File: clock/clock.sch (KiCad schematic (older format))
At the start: 4 parts, among them P101 CONN_01X03, P102 CONN_FAN_PWM, P103 CONN_02X08

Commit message: Place the reference designators.
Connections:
- net labels added: ~CARRIER_SRST~
- wire segments 129 -> 133
- no-connect marks 1 -> 0
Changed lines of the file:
@@
 F26 "TEMP_SDA" I R 3500 4500 60
 F27 "FAN_TACH" I L 2400 5500 60
+F28 "~CARRIER_SRST~" I L 2400 5000 60
 $EndSheet
 $Comp
@@
 	1    0    0    -1
 $EndComp
-NoConn ~ 1050 6900
 $Comp
 L PWR_FLAG #FLG07
@@
 Connection ~ 1700 2750
 Wire Wire Line
-	9950 1100 10050 1100
-Wire Wire Line
-	10050 1100 10050 1950
-Wire Wire Line
-	9950 1800 10050 1800
+	10050 1800 9950 1800
 Connection ~ 10050 1800
 Wire Wire Line
-	9950 1700 10050 1700
+	10050 1700 9950 1700
 Connection ~ 10050 1700
 Wire Wire Line
-	9950 1600 10050 1600
+	10050 1600 9950 1600
 Connection ~ 10050 1600
 Wire Wire Line
-	9950 1500 10050 1500
+	10050 1500 9950 1500
 Connection ~ 10050 1500
 Wire Wire Line
-	9950 1400 10050 1400
+	10050 1400 9950 1400
 Connection ~ 10050 1400
 Wire Wire Line
@@
 Wire Wire Line
 	9950 1200 10050 1200
-Connection ~ 10050 1200
 Wire Wire Line
 	9450 1100 9350 1100
@@
 Wire Wire Line
 	1300 7100 1050 7100
+Wire Wire Line
+	2400 900  1150 900
+Wire Wire Line
+	1150 900  1150 6900
+Wire Wire Line
+	1150 6900 1050 6900
+Wire Wire Line
+	2400 5000 550  5000
+Text Label 600  5000 0    50   ~ 0
+~CARRIER_SRST~
+Wire Wire Line
+	10050 1200 10050 1950
+Wire Wire Line
+	9950 1100 10550 1100
+Text Label 10000 1100 0    50   ~ 0
+~CARRIER_SRST~
 $EndSCHEMATC

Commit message: Correct spelling. Minor clean ups.
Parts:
- P101: Manufacturer (none) -> Phoenix Contact; PartNum (none) -> 1729131
- P103: Manufacturer (none) -> Omron Electronics; PartNum (none) -> XG4A-1631
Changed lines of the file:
@@
 F 2 "Connect:he10-16d" H 9700 250 60  0001 C CNN
 F 3 "" H 9700 250 60  0000 C CNN
+F 4 "Omron Electronics" H 9700 1450 50  0001 C CNN "Manufacturer"
+F 5 "XG4A-1631" H 9700 1450 50  0001 C CNN "PartNum"
 	1    9700 1450
 	1    0    0    -1
@@
 F 2 "local:Terminal_Block_1x03" H 850 7000 60  0001 C CNN
 F 3 "" H 850 7000 60  0000 C CNN
+F 4 "Phoenix Contact" H 850 7000 50  0001 C CNN "Manufacturer"
+F 5 "1729131" H 850 7000 50  0001 C CNN "PartNum"
 	1    850  7000
 	-1   0    0    1

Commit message: Change SOT-23 footprint. Move some vias onto grid.
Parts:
- P103: value CONN_02X08 -> XG4A-1631; footprint Connect:he10-16d -> local:XG4A-1631
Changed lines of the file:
@@
 P 9700 1450
 F 0 "P103" H 9700 1900 50  0000 C CNN
-F 1 "CONN_02X08" V 9700 1450 50  0000 C CNN
-F 2 "Connect:he10-16d" H 9700 250 60  0001 C CNN
+F 1 "XG4A-1631" V 9700 1450 50  0000 C CNN
+F 2 "local:XG4A-1631" H 9700 250 60  0001 C CNN
 F 3 "" H 9700 250 60  0000 C CNN
 F 4 "Omron Electronics" H 9700 1450 50  0001 C CNN "Manufacturer"

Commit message: Lock all the stitching vias. Remove FVXO alternate to OCXO.
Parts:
- removed P103: XG4A-1631, local:XG4A-1631, symbol CONN_02X08
- added P103: XG4A-1631, local:XG4A-1631, symbol CONN_02X08_MTG
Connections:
- wire segments 133 -> 136
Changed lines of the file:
@@
 $EndSheet
-$Comp
-L CONN_02X08 P103
-U 1 1 5632C7F9
-P 9700 1450
-F 0 "P103" H 9700 1900 50  0000 C CNN
-F 1 "XG4A-1631" V 9700 1450 50  0000 C CNN
-F 2 "local:XG4A-1631" H 9700 250 60  0001 C CNN
-F 3 "" H 9700 250 60  0000 C CNN
-F 4 "Omron Electronics" H 9700 1450 50  0001 C CNN "Manufacturer"
-F 5 "XG4A-1631" H 9700 1450 50  0001 C CNN "PartNum"
-	1    9700 1450
-	1    0    0    -1
-$EndComp
 $Comp
 L GND #PWR03
@@
 	9450 1100 9350 1100
 Wire Wire Line
-	9350 1100 9350 1950
-Wire Wire Line
 	9450 1600 9350 1600
-Connection ~ 9350 1600
 Wire Wire Line
 	3550 1500 4700 1500
@@
 ~CARRIER_SRST~
 Wire Wire Line
-	10050 1200 10050 1950
-Wire Wire Line
-	9950 1100 10550 1100
-Text Label 10000 1100 0    50   ~ 0
+	10050 1100 10050 1950
+Wire Wire Line
+	9350 850  9950 850
+Text Label 9400 850  0    50   ~ 0
 ~CARRIER_SRST~
+$Comp
+L CONN_02X08_MTG P103
+U 1 1 566653AD
+P 9700 1450
+F 0 "P103" H 9700 1900 50  0000 C CNN
+F 1 "XG4A-1631" V 9700 1450 50  0000 C CNN
+F 2 "local:XG4A-1631" H 9700 250 60  0001 C CNN
+F 3 "" H 9700 250 60  0000 C CNN
+F 4 "Omron Electronics" H 9700 1450 60  0001 C CNN "Manufacturer"
+F 5 "XG4A-1631" H 9700 1450 60  0001 C CNN "PartNum"
+	1    9700 1450
+	1    0    0    -1
+$EndComp
+$Comp
+L GND #PWR09
+U 1 1 56670FE1
+P 9700 2100
+F 0 "#PWR09" H 9700 1850 50  0001 C CNN
+F 1 "GND" H 9700 1950 50  0000 C CNN
+F 2 "" H 9700 2100 60  0000 C CNN
+F 3 "" H 9700 2100 60  0000 C CNN
+	1    9700 2100
+	1    0    0    -1
+$EndComp
+Wire Wire Line
+	9700 2100 9700 2000
+Wire Wire Line
+	9350 1100 9350 850
+Wire Wire Line
+	9950 1100 10050 1100
+Connection ~ 10050 1200
+Wire Wire Line
+	9350 1600 9350 1950
 $EndSCHEMATC

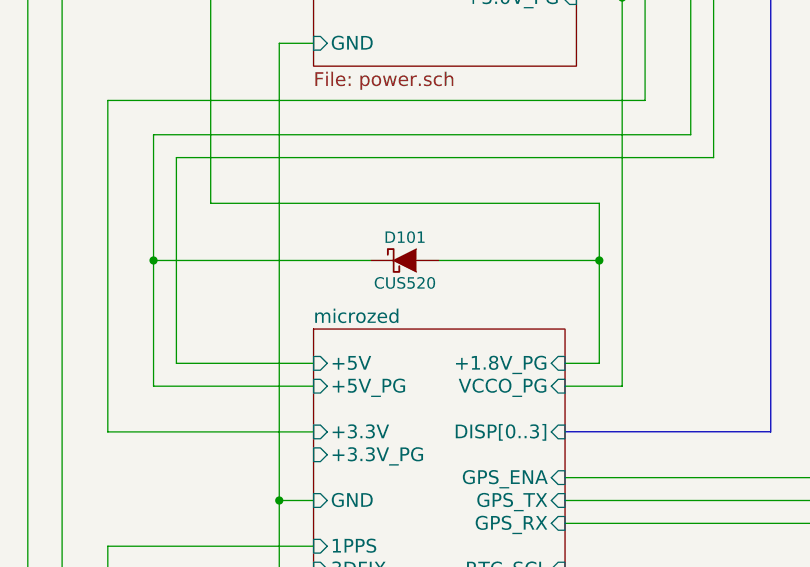
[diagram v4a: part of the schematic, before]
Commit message: Add second capacitor to 3V LDO input. Add series resistor to LDO enable.
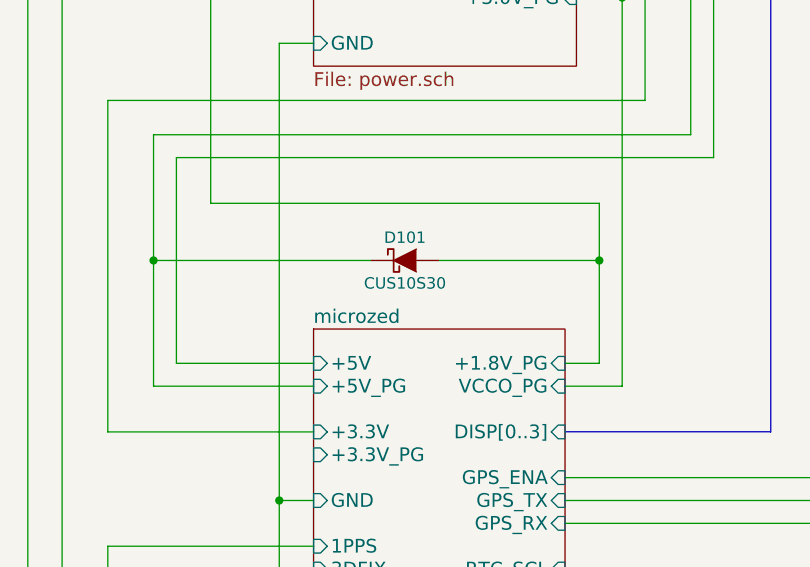
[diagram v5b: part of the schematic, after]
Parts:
- D101: value CUS520 -> CUS10S30; PartNum CUS520 -> CUS10S30
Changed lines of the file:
@@
 P 2800 2750
 F 0 "D101" H 2800 2850 50  0000 C CNN
-F 1 "CUS520" H 2800 2650 50  0000 C CNN
+F 1 "CUS10S30" H 2800 2650 50  0000 C CNN
 F 2 "local:SOD-323_USC" H 2800 2750 60  0001 C CNN
 F 3 "" H 2800 2750 60  0000 C CNN
 F 4 "Toshiba" H 2800 2750 50  0001 C CNN "Manufacturer"
-F 5 "CUS520" H 2800 2750 60  0001 C CNN "PartNum"
+F 5 "CUS10S30" H 2800 2750 60  0001 C CNN "PartNum"
 	1    2800 2750
 	1    0    0    -1

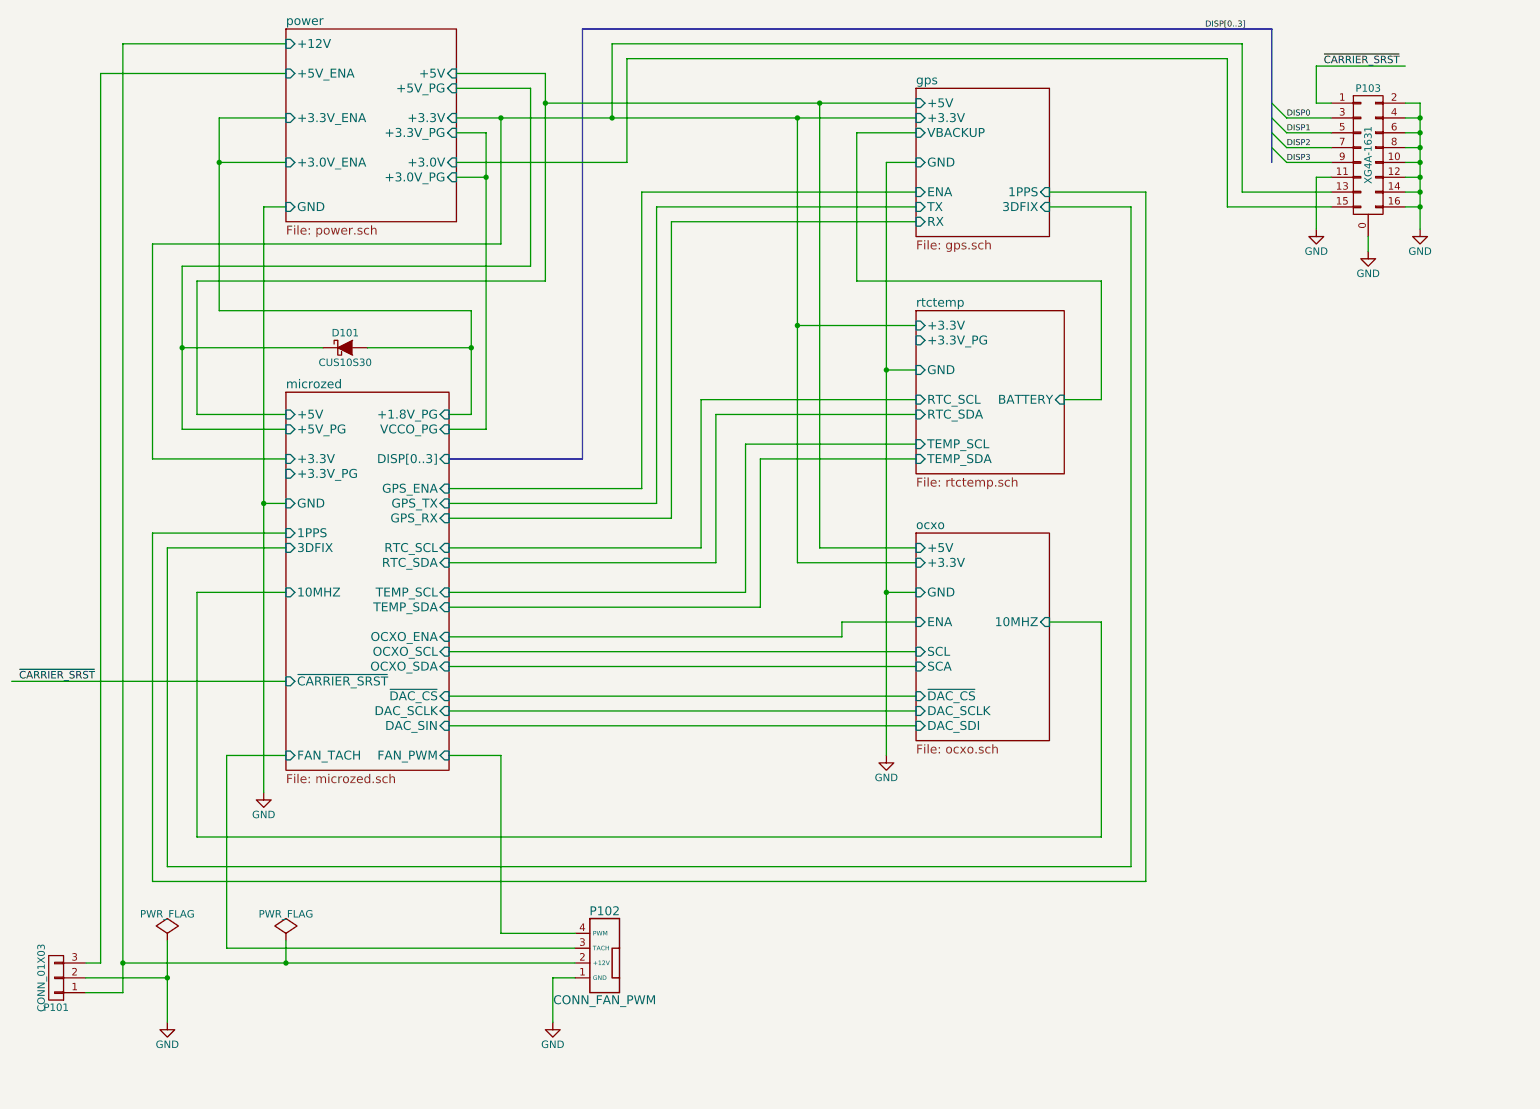
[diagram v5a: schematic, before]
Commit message: Preliminary changes from lab bring up.   Properly connect ref2 on PCA9306.   Duplicate +5V power good to drive +3.3V converter.   Change gain structure on OCXO control voltage drive.   Add FET control to disable linear regulators.
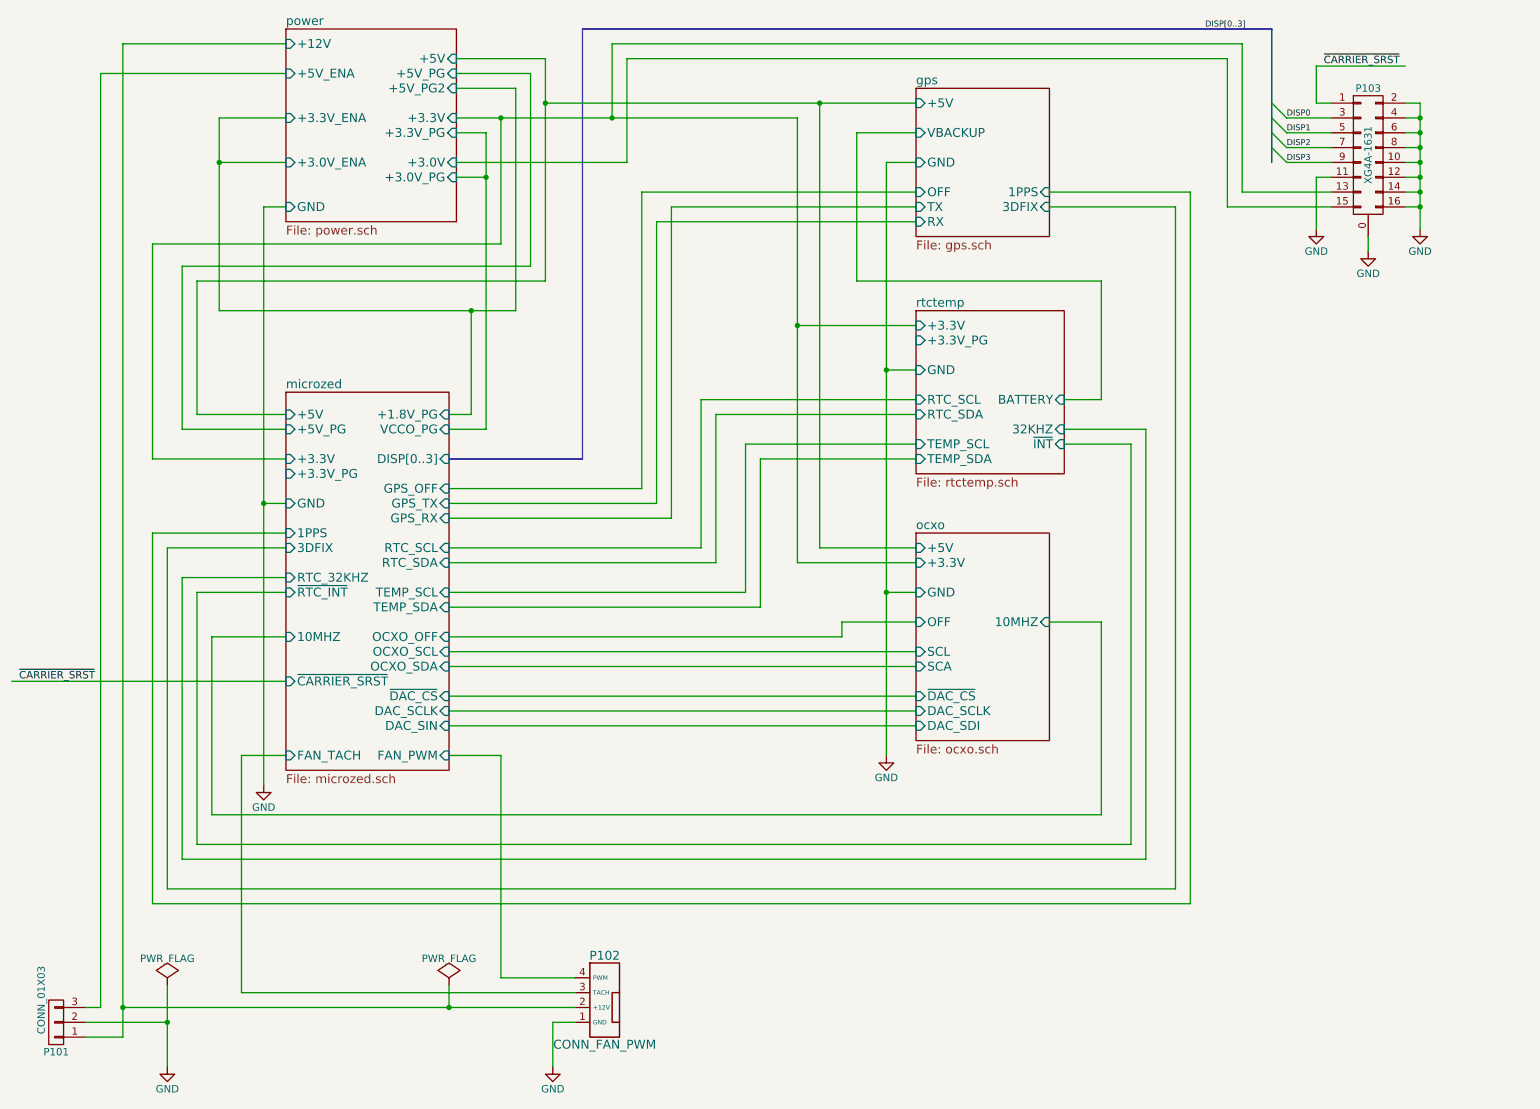
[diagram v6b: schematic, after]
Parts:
- removed D101: CUS10S30, local:SOD-323_USC, symbol D_Schottky
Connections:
- net gps/+3.3V renamed microzed/+3.3V
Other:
- moved on the sheet: P101, P102
